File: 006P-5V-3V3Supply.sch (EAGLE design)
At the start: 15 parts, among them IC1 7805T, IC2 TM48M033F

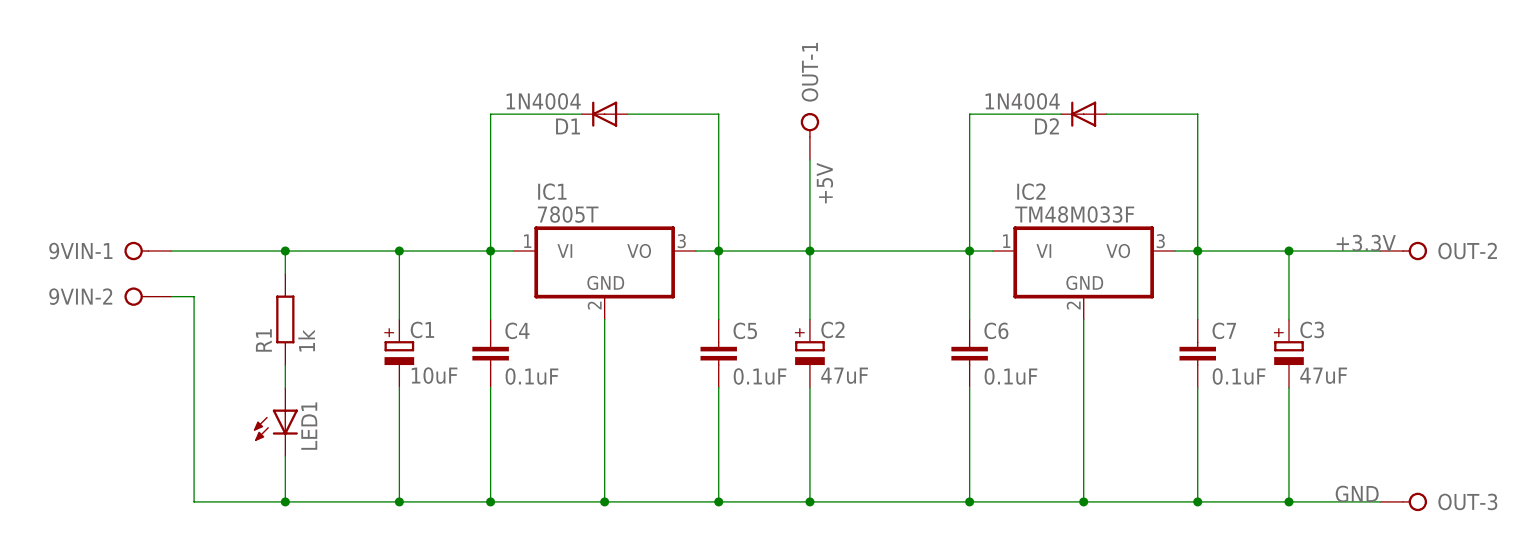
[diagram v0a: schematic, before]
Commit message: 回路図、基板図を修正
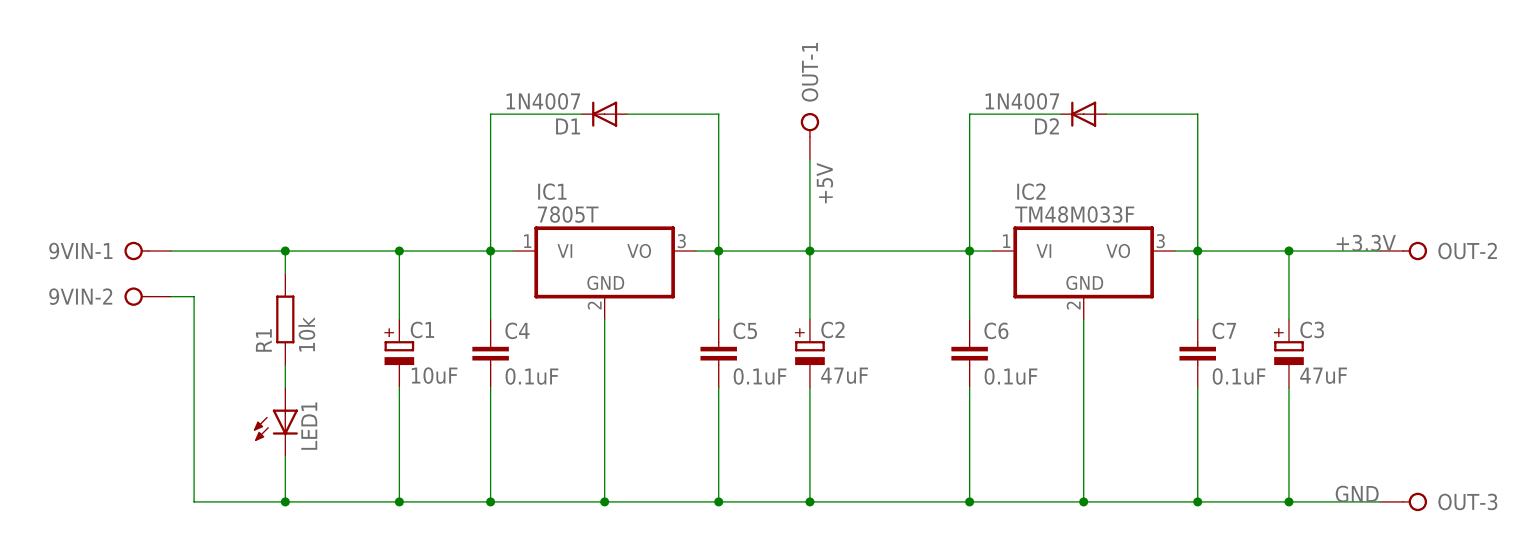
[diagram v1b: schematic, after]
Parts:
- D1, D2: value 1N4004 -> 1N4007
- R1: value 1k -> 10k
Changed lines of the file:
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@@
 <part name="IC1" library="linear" deviceset="78*" device="T" technology="05"/>
 <part name="IC2" library="linear" deviceset="78*" device="TV" technology="05" value="TM48M033F"/>
-<part name="D1" library="diode" deviceset="1N4004" device=""/>
-<part name="D2" library="diode" deviceset="1N4004" device=""/>
+<part name="D1" library="diode" deviceset="1N4004" device="" value="1N4007"/>
+<part name="D2" library="diode" deviceset="1N4004" device="" value="1N4007"/>
 <part name="C1" library="rcl" deviceset="CPOL-EU" device="TT2D4L" value="10uF"/>
 <part name="C2" library="rcl" deviceset="CPOL-EU" device="TT2D5L" value="47uF"/>
@@
 <part name="C7" library="rcl" deviceset="C-EU" device="025-024X044" value="0.1uF"/>
 <part name="OUT" library="con-wago-508" deviceset="W237-03P" device=""/>
-<part name="R1" library="rcl" deviceset="R-EU_" device="0207/7" value="1k"/>
+<part name="R1" library="rcl" deviceset="R-EU_" device="0207/7" value="10k"/>
 <part name="LED1" library="led" deviceset="LED" device="3MM"/>
 <part name="9VIN" library="con-wago-508" deviceset="W237-02P" device=""/>
